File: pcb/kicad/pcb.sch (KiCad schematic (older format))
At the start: 226 parts, among them J1 MX-NoLED, K0 MX-NoLED, K1 MX-NoLED, K10 MX-NoLED, K2 MX-NoLED, K3 MX-NoLED, K4 MX-NoLED, K5 MX-NoLED, K6 MX-NoLED, K7 MX-NoLED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

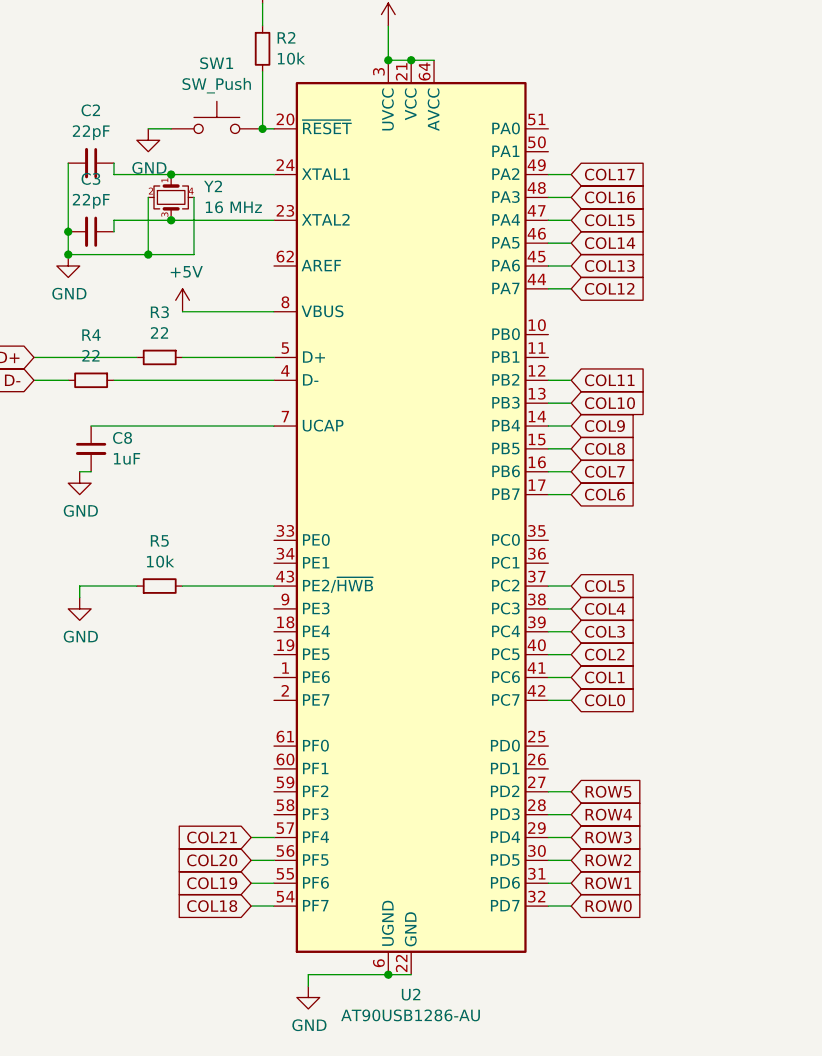
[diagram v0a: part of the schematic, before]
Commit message: pcb: position components
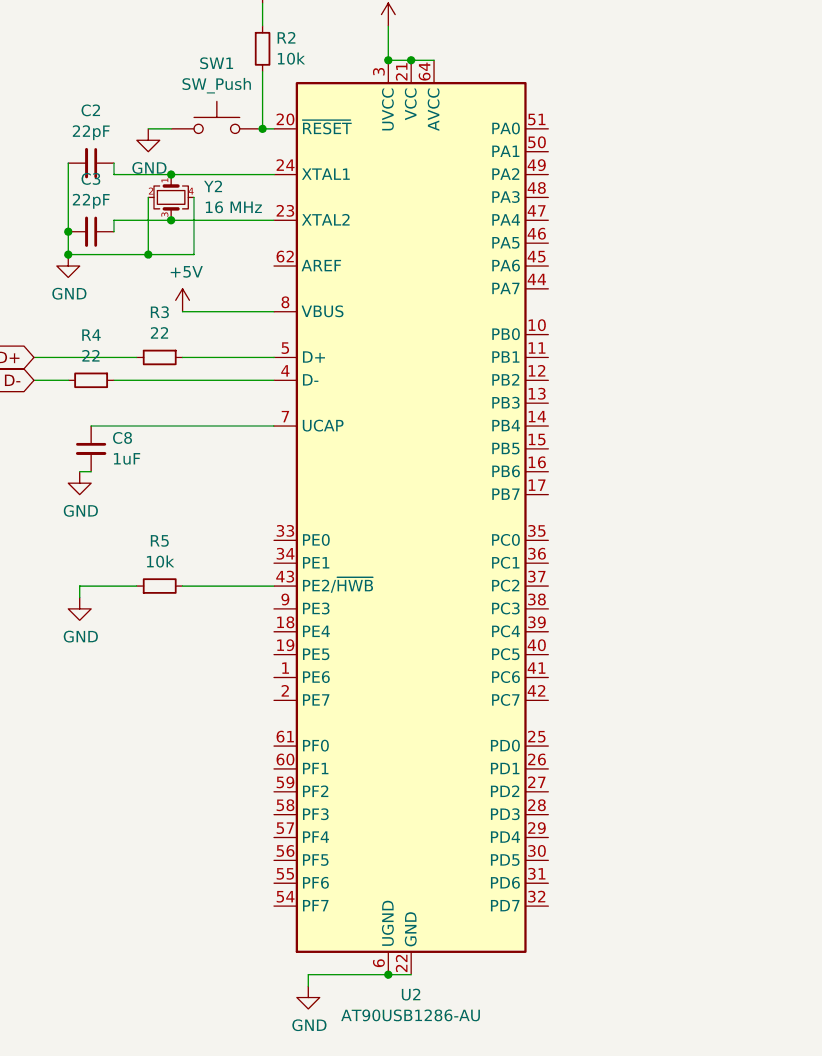
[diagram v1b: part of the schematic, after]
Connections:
- net COL0: no longer U2.42 (PC7)
- net COL1: no longer U2.41 (PC6)
- net COL10: no longer U2.13 (PB3)
- net COL11: no longer U2.12 (PB2)
- net COL12: no longer U2.44 (PA7)
- net COL13: no longer U2.45 (PA6)
- net COL14: no longer U2.46 (PA5)
- net COL15: no longer U2.47 (PA4)
- net COL16: no longer U2.48 (PA3)
- net COL17: no longer U2.49 (PA2)
- net COL18: no longer U2.54 (PF7)
- net COL19: no longer U2.55 (PF6)
- net COL2: no longer U2.40 (PC5)
- net COL20: no longer U2.56 (PF5)
- net COL21: no longer U2.57 (PF4)
- net COL3: no longer U2.39 (PC4)
- net COL4: no longer U2.38 (PC3)
- net COL5: no longer U2.37 (PC2)
- net COL6: no longer U2.17 (PB7)
- net COL7: no longer U2.16 (PB6)
- net COL8: no longer U2.15 (PB5)
- net COL9: no longer U2.14 (PB4)
- net ROW0: no longer U2.32 (PD7)
- net ROW1: no longer U2.31 (PD6)
- net ROW2: no longer U2.30 (PD5)
- net ROW3: no longer U2.29 (PD4)
- net ROW4: no longer U2.28 (PD3)
- net ROW5: no longer U2.27 (PD2)
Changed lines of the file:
@@
 Text GLabel 10650 750  1    50   Input ~ 0
 COL21
-Text GLabel 5550 8750 2    50   Input ~ 0
-ROW0
-Text GLabel 5550 8650 2    50   Input ~ 0
-ROW1
-Text GLabel 5550 8550 2    50   Input ~ 0
-ROW2
-Text GLabel 5550 8450 2    50   Input ~ 0
-ROW3
-Text GLabel 5550 8350 2    50   Input ~ 0
-ROW4
-Text GLabel 5550 8250 2    50   Input ~ 0
-ROW5
-Wire Wire Line
-	5450 8750 5550 8750
-Wire Wire Line
-	5450 8650 5550 8650
-Wire Wire Line
-	5450 8550 5550 8550
-Wire Wire Line
-	5450 8450 5550 8450
-Wire Wire Line
-	5450 8350 5550 8350
-Wire Wire Line
-	5450 8250 5550 8250
-Text GLabel 5550 7850 2    50   Input ~ 0
-COL0
-Text GLabel 5550 7750 2    50   Input ~ 0
-COL1
-Text GLabel 5550 7650 2    50   Input ~ 0
-COL2
-Text GLabel 5550 7550 2    50   Input ~ 0
-COL3
-Text GLabel 5550 7450 2    50   Input ~ 0
-COL4
-Text GLabel 5550 7350 2    50   Input ~ 0
-COL5
-Text GLabel 5550 6950 2    50   Input ~ 0
-COL6
-Text GLabel 5550 6850 2    50   Input ~ 0
-COL7
-Text GLabel 5550 6750 2    50   Input ~ 0
-COL8
-Text GLabel 5550 6650 2    50   Input ~ 0
-COL9
-Text GLabel 5550 6550 2    50   Input ~ 0
-COL10
-Text GLabel 5550 6050 2    50   Input ~ 0
-COL12
-Text GLabel 5550 5950 2    50   Input ~ 0
-COL13
-Text GLabel 5550 5850 2    50   Input ~ 0
-COL14
-Text GLabel 5550 5750 2    50   Input ~ 0
-COL15
-Text GLabel 5550 6450 2    50   Input ~ 0
-COL11
-Text GLabel 5550 5650 2    50   Input ~ 0
-COL16
-Text GLabel 5550 5550 2    50   Input ~ 0
-COL17
-Text GLabel 4150 8750 0    50   Input ~ 0
-COL18
-Text GLabel 4150 8650 0    50   Input ~ 0
-COL19
-Text GLabel 4150 8550 0    50   Input ~ 0
-COL20
-Text GLabel 4150 8450 0    50   Input ~ 0
-COL21
-Wire Wire Line
-	5550 7850 5450 7850
-Wire Wire Line
-	5450 7750 5550 7750
-Wire Wire Line
-	5550 7650 5450 7650
-Wire Wire Line
-	5450 7550 5550 7550
-Wire Wire Line
-	5550 7450 5450 7450
-Wire Wire Line
-	5450 7350 5550 7350
-Wire Wire Line
-	5450 6950 5550 6950
-Wire Wire Line
-	5450 6850 5550 6850
-Wire Wire Line
-	5550 6750 5450 6750
-Wire Wire Line
-	5450 6650 5550 6650
-Wire Wire Line
-	5550 6550 5450 6550
-Wire Wire Line
-	5450 6450 5550 6450
-Wire Wire Line
-	5550 6050 5450 6050
-Wire Wire Line
-	5450 5950 5550 5950
-Wire Wire Line
-	5550 5850 5450 5850
-Wire Wire Line
-	5450 5750 5550 5750
-Wire Wire Line
-	5550 5650 5450 5650
-Wire Wire Line
-	5450 5550 5550 5550
-Wire Wire Line
-	4150 8750 4250 8750
-Wire Wire Line
-	4150 8650 4250 8650
-Wire Wire Line
-	4250 8550 4150 8550
-Wire Wire Line
-	4150 8450 4250 8450
 $EndSCHEMATC

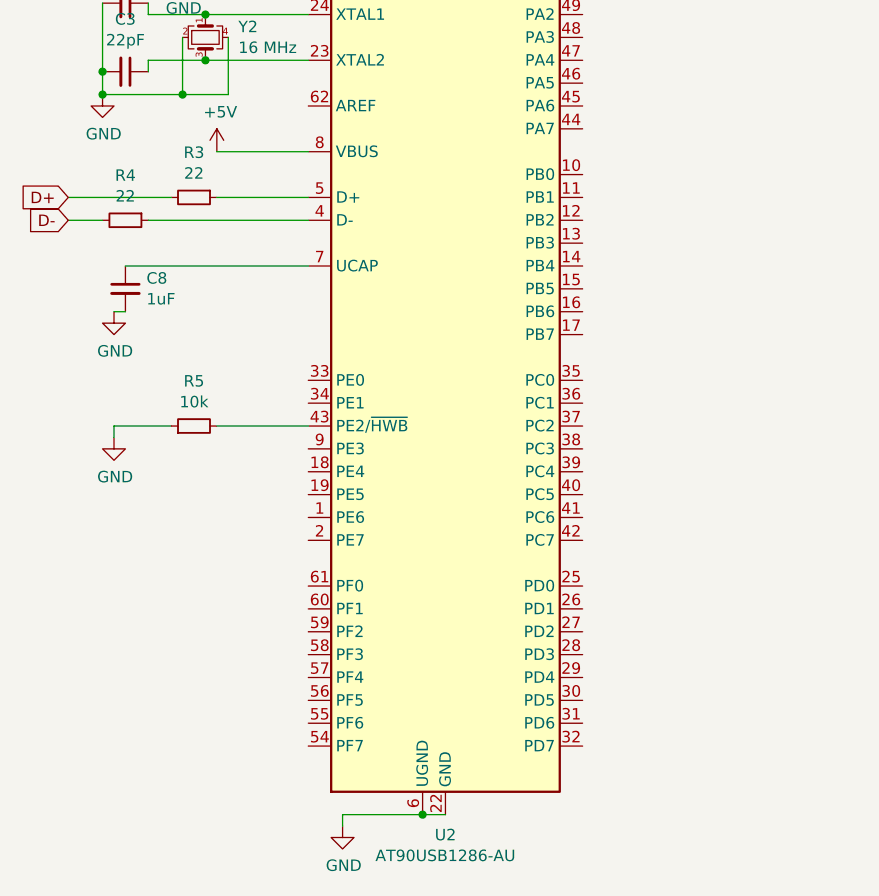
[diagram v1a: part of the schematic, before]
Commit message: pcb: finish mcu positioning
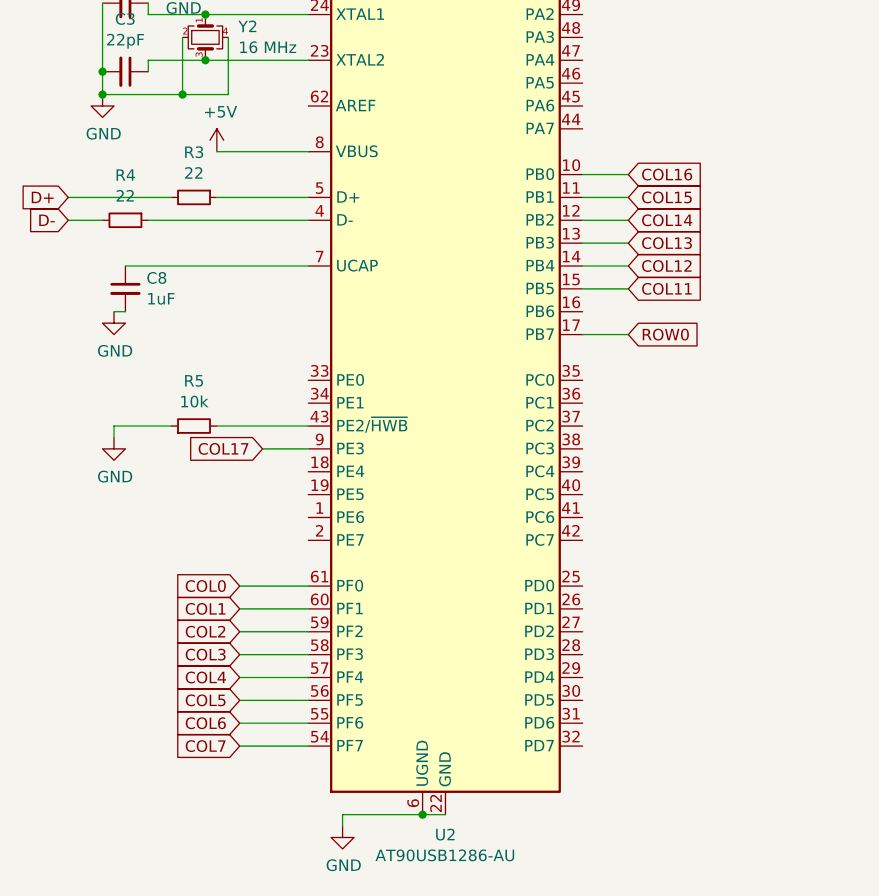
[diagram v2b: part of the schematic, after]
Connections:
- net COL0: now also U2.61 (PF0)
- net COL1: now also U2.60 (PF1)
- net COL11: now also U2.15 (PB5)
- net COL12: now also U2.14 (PB4)
- net COL13: now also U2.13 (PB3)
- net COL14: now also U2.12 (PB2)
- net COL15: now also U2.11 (PB1)
- net COL16: now also U2.10 (PB0)
- net COL17: now also U2.9 (PE3)
- net COL2: now also U2.59 (PF2)
- net COL3: now also U2.58 (PF3)
- net COL4: now also U2.57 (PF4)
- net COL5: now also U2.56 (PF5)
- net COL6: now also U2.55 (PF6)
- net COL7: now also U2.54 (PF7)
- net ROW0: now also U2.17 (PB7)
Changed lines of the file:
@@
 Text GLabel 10650 750  1    50   Input ~ 0
 COL21
+Text GLabel 4050 7450 0    50   Input ~ 0
+COL17
+Wire Wire Line
+	4050 7450 4250 7450
+Text GLabel 5650 6250 2    50   Input ~ 0
+COL16
+Text GLabel 5650 6350 2    50   Input ~ 0
+COL15
+Text GLabel 5650 6450 2    50   Input ~ 0
+COL14
+Text GLabel 5650 6550 2    50   Input ~ 0
+COL13
+Text GLabel 5650 6650 2    50   Input ~ 0
+COL12
+Text GLabel 5650 6750 2    50   Input ~ 0
+COL11
+Text GLabel 5650 6950 2    50   Input ~ 0
+ROW0
+Wire Wire Line
+	5650 6250 5450 6250
+Wire Wire Line
+	5450 6350 5650 6350
+Wire Wire Line
+	5650 6450 5450 6450
+Wire Wire Line
+	5450 6550 5650 6550
+Wire Wire Line
+	5650 6650 5450 6650
+Wire Wire Line
+	5450 6750 5650 6750
+Wire Wire Line
+	5450 6950 5650 6950
+Text GLabel 3950 8050 0    50   Input ~ 0
+COL0
+Text GLabel 3950 8150 0    50   Input ~ 0
+COL1
+Text GLabel 3950 8250 0    50   Input ~ 0
+COL2
+Text GLabel 3950 8350 0    50   Input ~ 0
+COL3
+Text GLabel 3950 8450 0    50   Input ~ 0
+COL4
+Text GLabel 3950 8550 0    50   Input ~ 0
+COL5
+Text GLabel 3950 8650 0    50   Input ~ 0
+COL6
+Text GLabel 3950 8750 0    50   Input ~ 0
+COL7
+Wire Wire Line
+	3950 8050 4250 8050
+Wire Wire Line
+	3950 8150 4250 8150
+Wire Wire Line
+	3950 8250 4250 8250
+Wire Wire Line
+	3950 8350 4250 8350
+Wire Wire Line
+	3950 8450 4250 8450
+Wire Wire Line
+	3950 8550 4250 8550
+Wire Wire Line
+	3950 8650 4250 8650
+Wire Wire Line
+	3950 8750 4250 8750
 $EndSCHEMATC

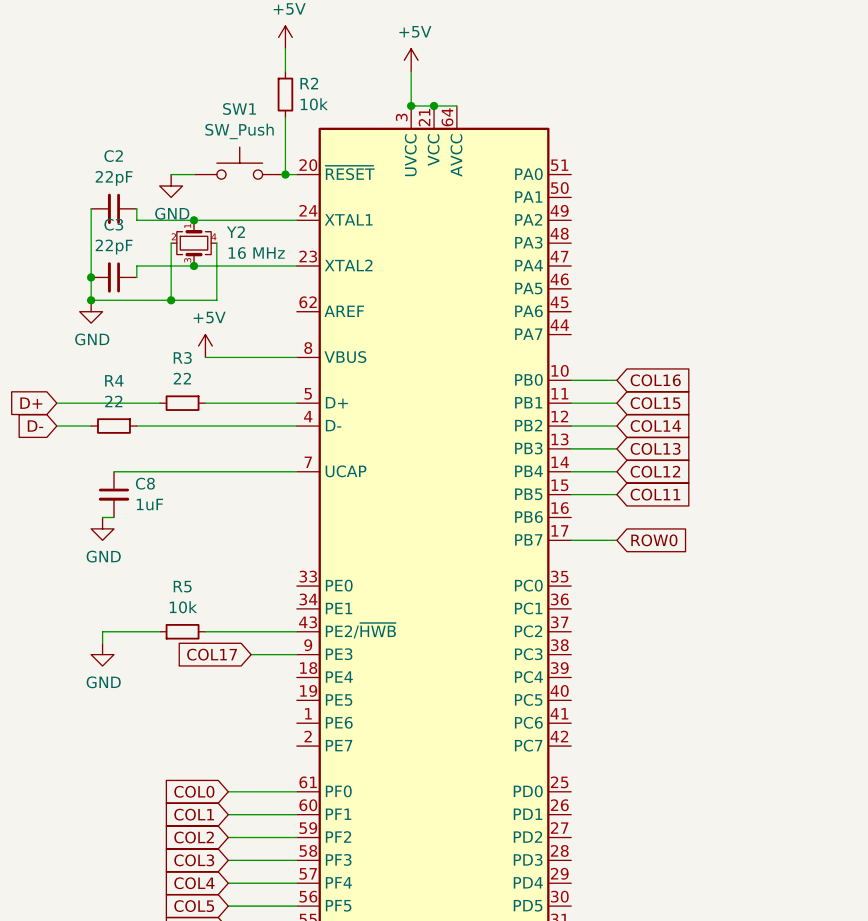
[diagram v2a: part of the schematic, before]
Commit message: pcb: finish tracks on pcb
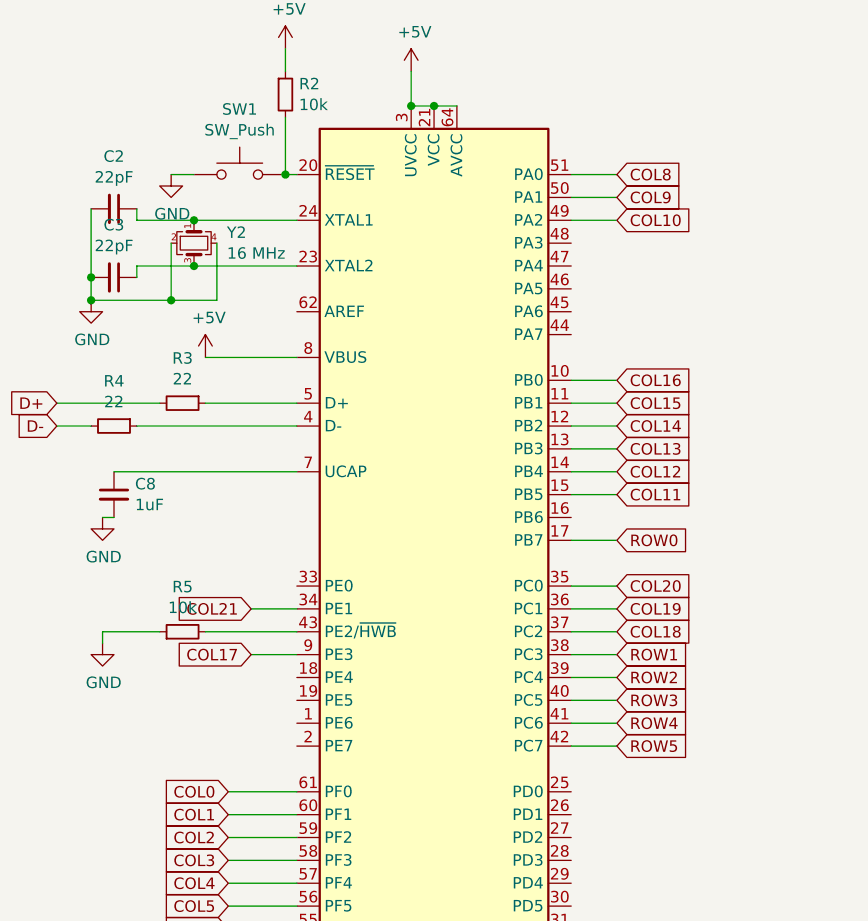
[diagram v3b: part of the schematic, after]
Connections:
- net COL10: now also U2.49 (PA2)
- net COL18: now also U2.37 (PC2)
- net COL19: now also U2.36 (PC1)
- net COL20: now also U2.35 (PC0)
- net COL21: now also U2.34 (PE1)
- net COL8: now also U2.51 (PA0)
- net COL9: now also U2.50 (PA1)
- net ROW1: now also U2.38 (PC3)
- net ROW2: now also U2.39 (PC4)
- net ROW3: now also U2.40 (PC5)
- net ROW4: now also U2.41 (PC6)
- net ROW5: now also U2.42 (PC7)
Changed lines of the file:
@@
 Wire Wire Line
 	3950 8750 4250 8750
+Text GLabel 5650 5350 2    50   Input ~ 0
+COL8
+Text GLabel 5650 5450 2    50   Input ~ 0
+COL9
+Text GLabel 5650 5550 2    50   Input ~ 0
+COL10
+Wire Wire Line
+	5450 5350 5650 5350
+Wire Wire Line
+	5650 5450 5450 5450
+Wire Wire Line
+	5450 5550 5650 5550
+Text GLabel 5650 7850 2    50   Input ~ 0
+ROW5
+Text GLabel 5650 7750 2    50   Input ~ 0
+ROW4
+Text GLabel 5650 7650 2    50   Input ~ 0
+ROW3
+Text GLabel 5650 7550 2    50   Input ~ 0
+ROW2
+Text GLabel 5650 7450 2    50   Input ~ 0
+ROW1
+Wire Wire Line
+	5450 7450 5650 7450
+Wire Wire Line
+	5650 7550 5450 7550
+Wire Wire Line
+	5450 7650 5650 7650
+Wire Wire Line
+	5650 7750 5450 7750
+Wire Wire Line
+	5450 7850 5650 7850
+Text GLabel 5650 7350 2    50   Input ~ 0
+COL18
+Text GLabel 5650 7250 2    50   Input ~ 0
+COL19
+Text GLabel 5650 7150 2    50   Input ~ 0
+COL20
+Wire Wire Line
+	5650 7150 5450 7150
+Wire Wire Line
+	5450 7250 5650 7250
+Wire Wire Line
+	5650 7350 5450 7350
+Text GLabel 4050 7250 0    50   Input ~ 0
+COL21
+Wire Wire Line
+	4050 7250 4250 7250
 $EndSCHEMATC
